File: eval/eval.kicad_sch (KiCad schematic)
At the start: 5 parts, among them J1 TC2030, U9 STM32G0B1CBTx

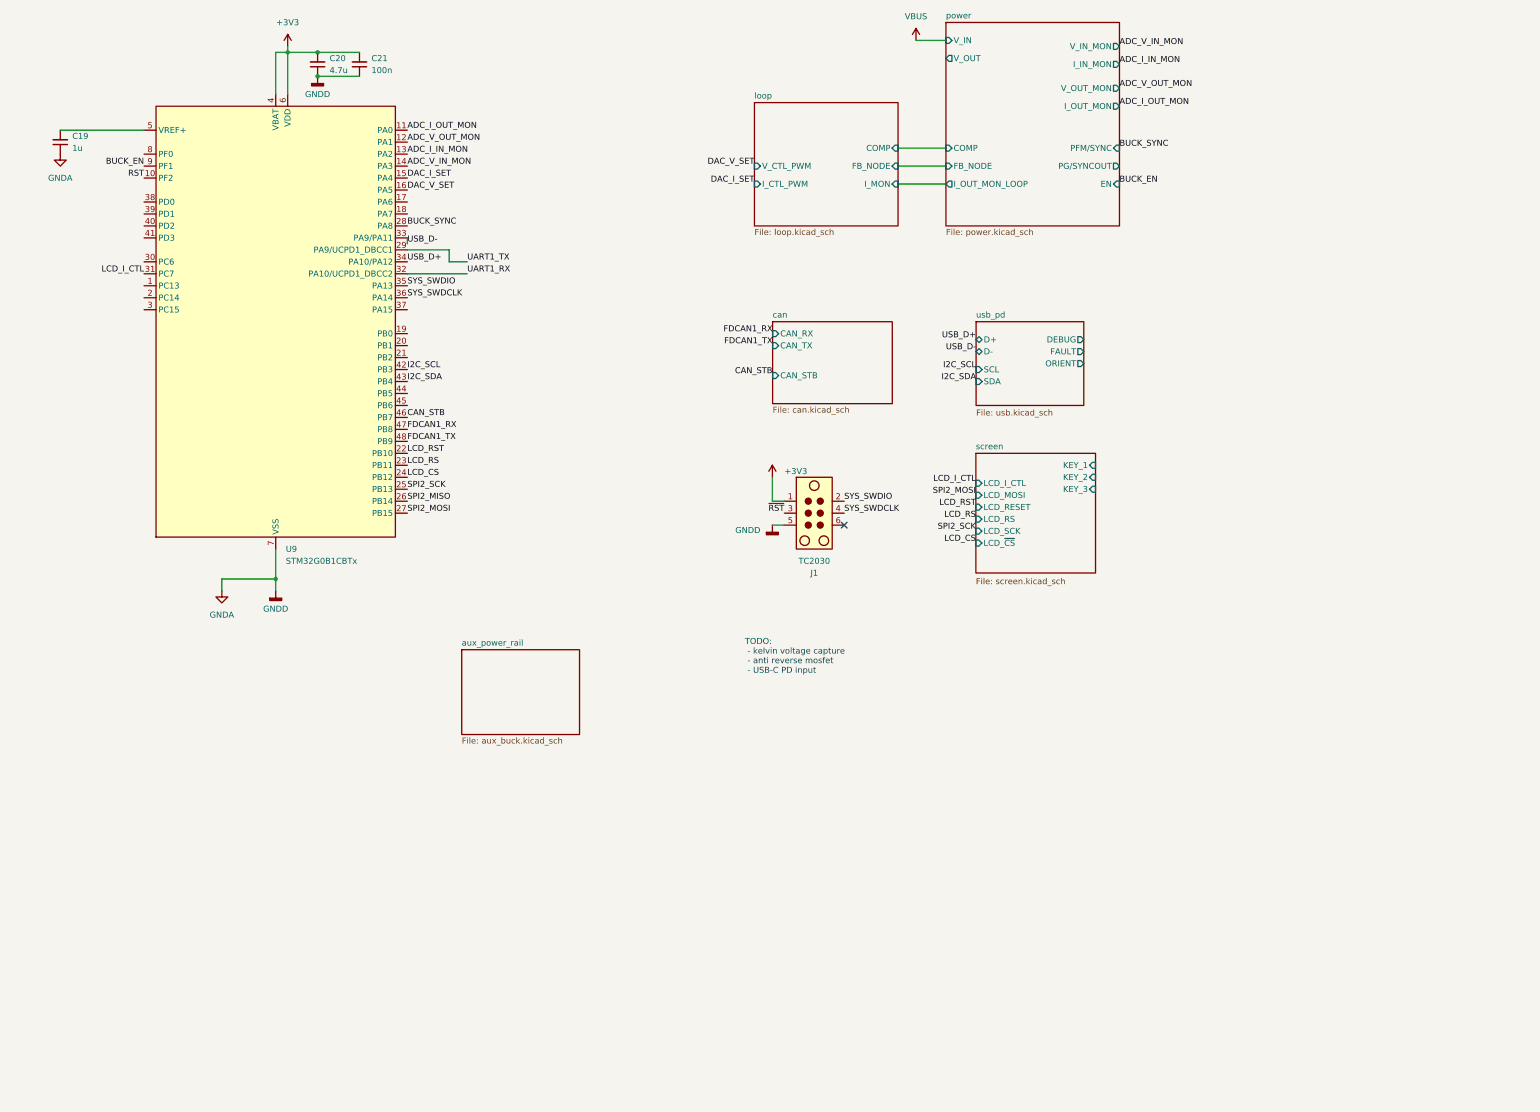
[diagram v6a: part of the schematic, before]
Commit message: [sch] Add ORing for 2 input
plan to add back to back mos protection for output (high side mos)
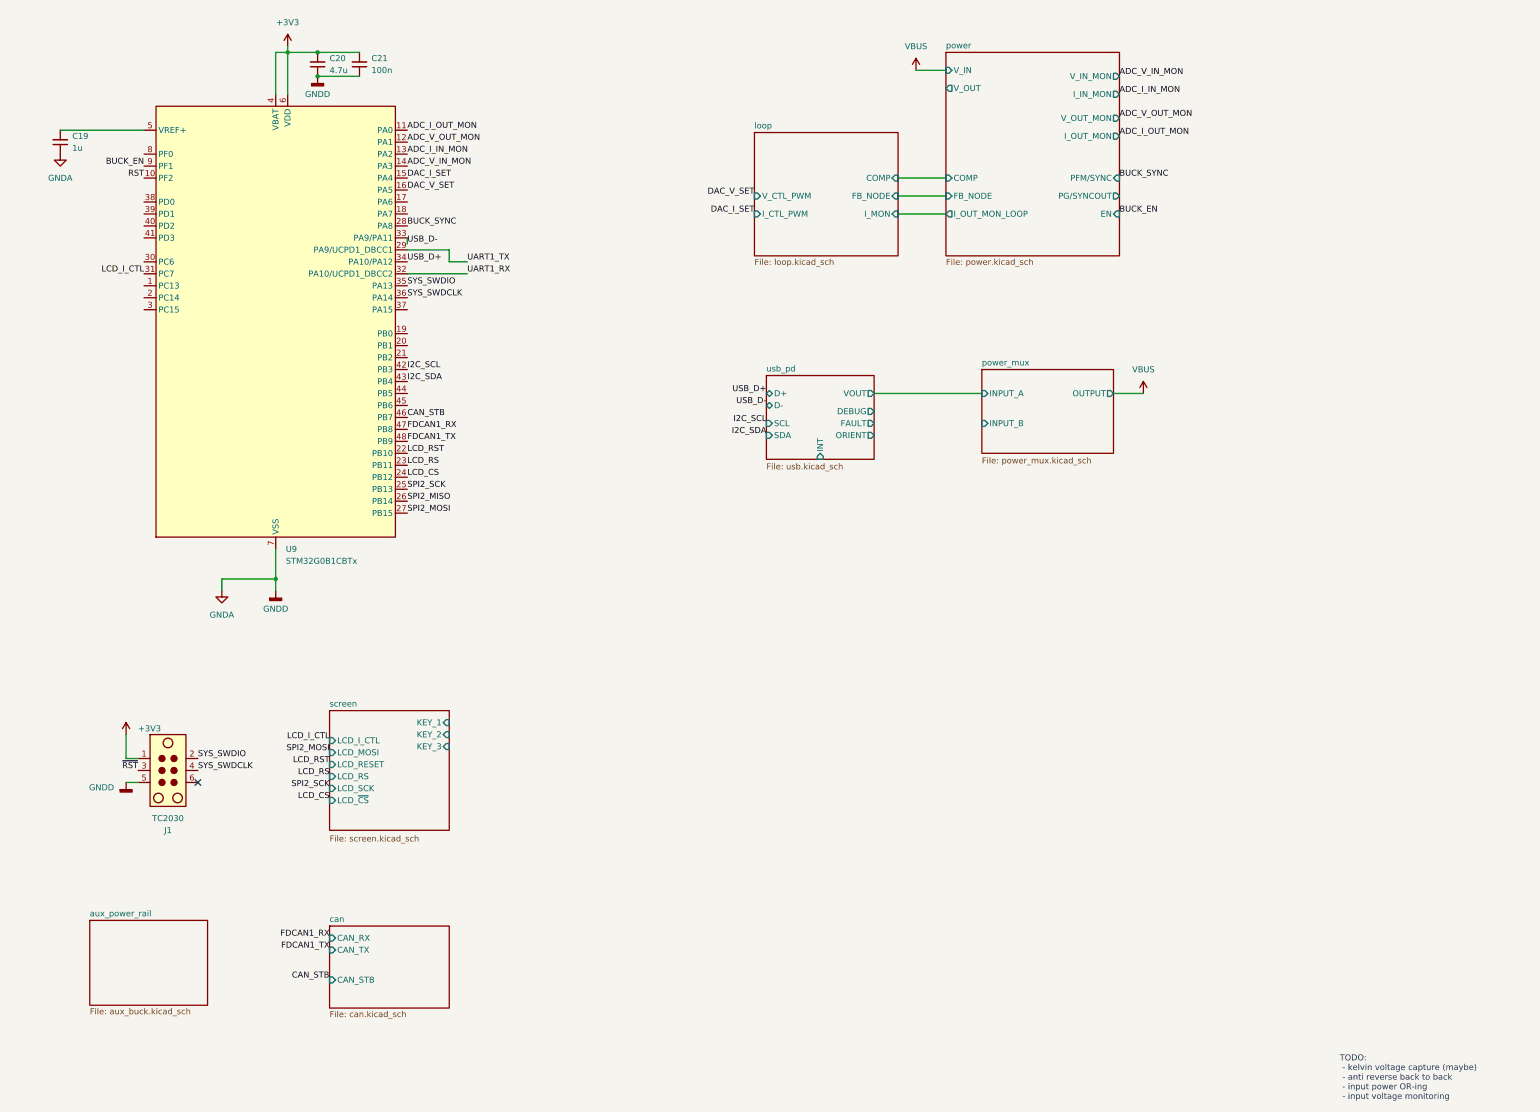
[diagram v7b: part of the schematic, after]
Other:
- added sheet power_mux (power_mux.kicad_sch)
- sheet usb_pd ports: added INT, VOUT; removed none
- note added: "TODO: - kelvin voltage capture (maybe) - anti reverse back to back - input power OR-ing - input voltage monitoring"
- note removed: "TODO: - kelvin voltage capture - anti reverse mosfet - USB-C PD input"
- moved on the sheet: J1

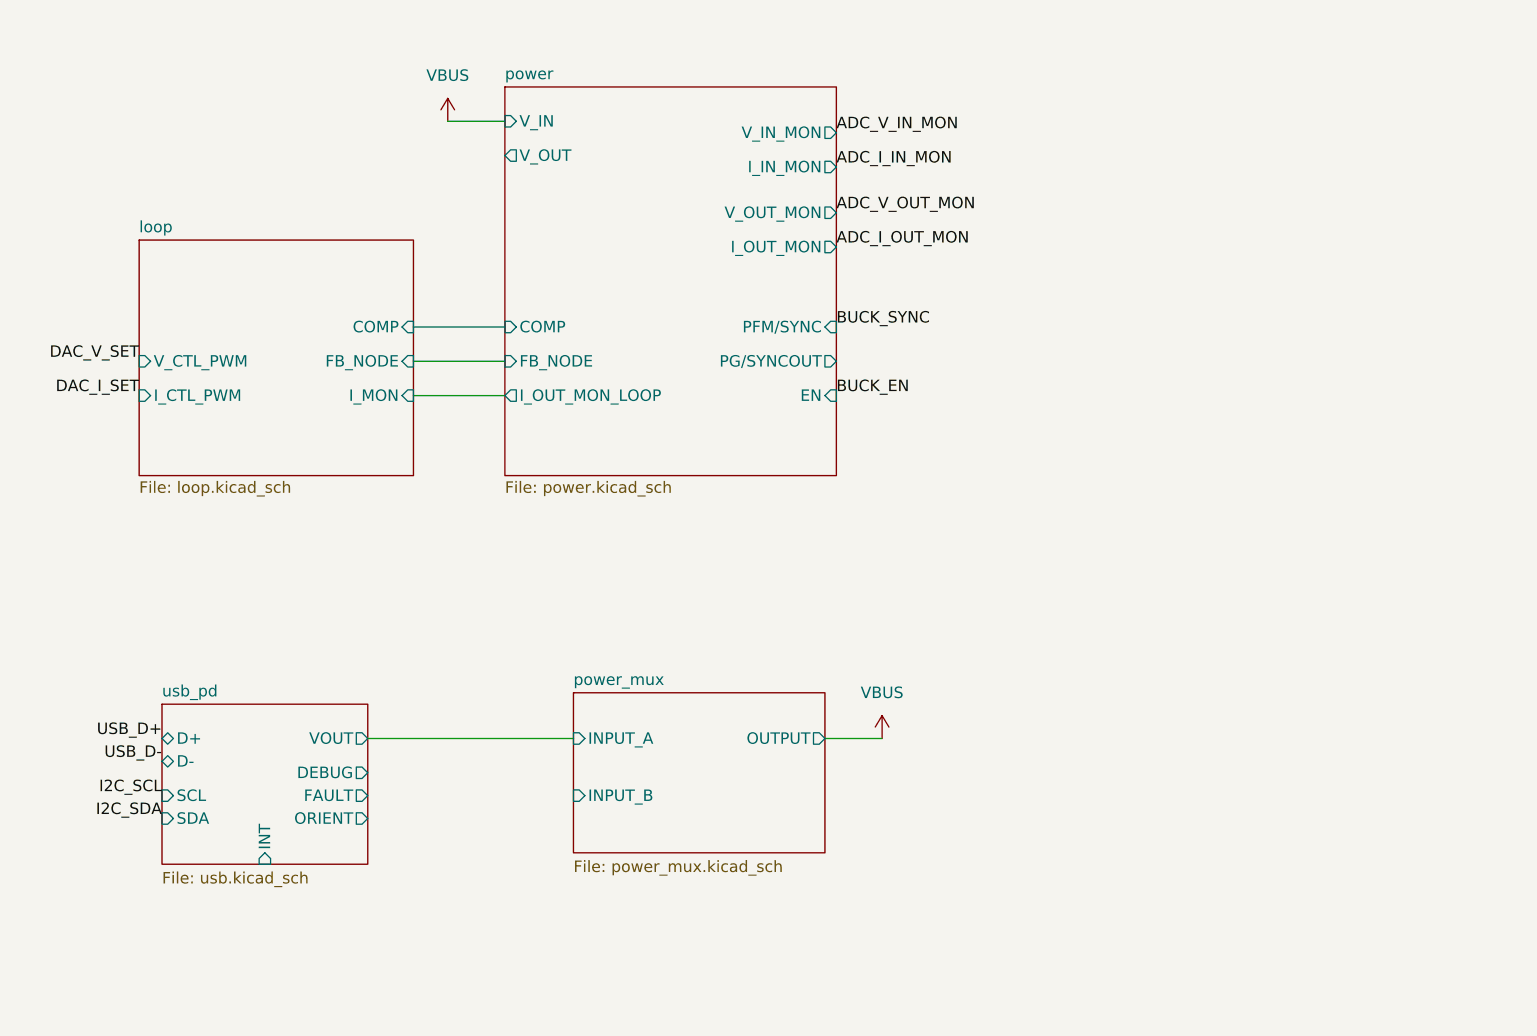
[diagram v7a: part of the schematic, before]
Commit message: [sch] add back to back protection (MX74502)
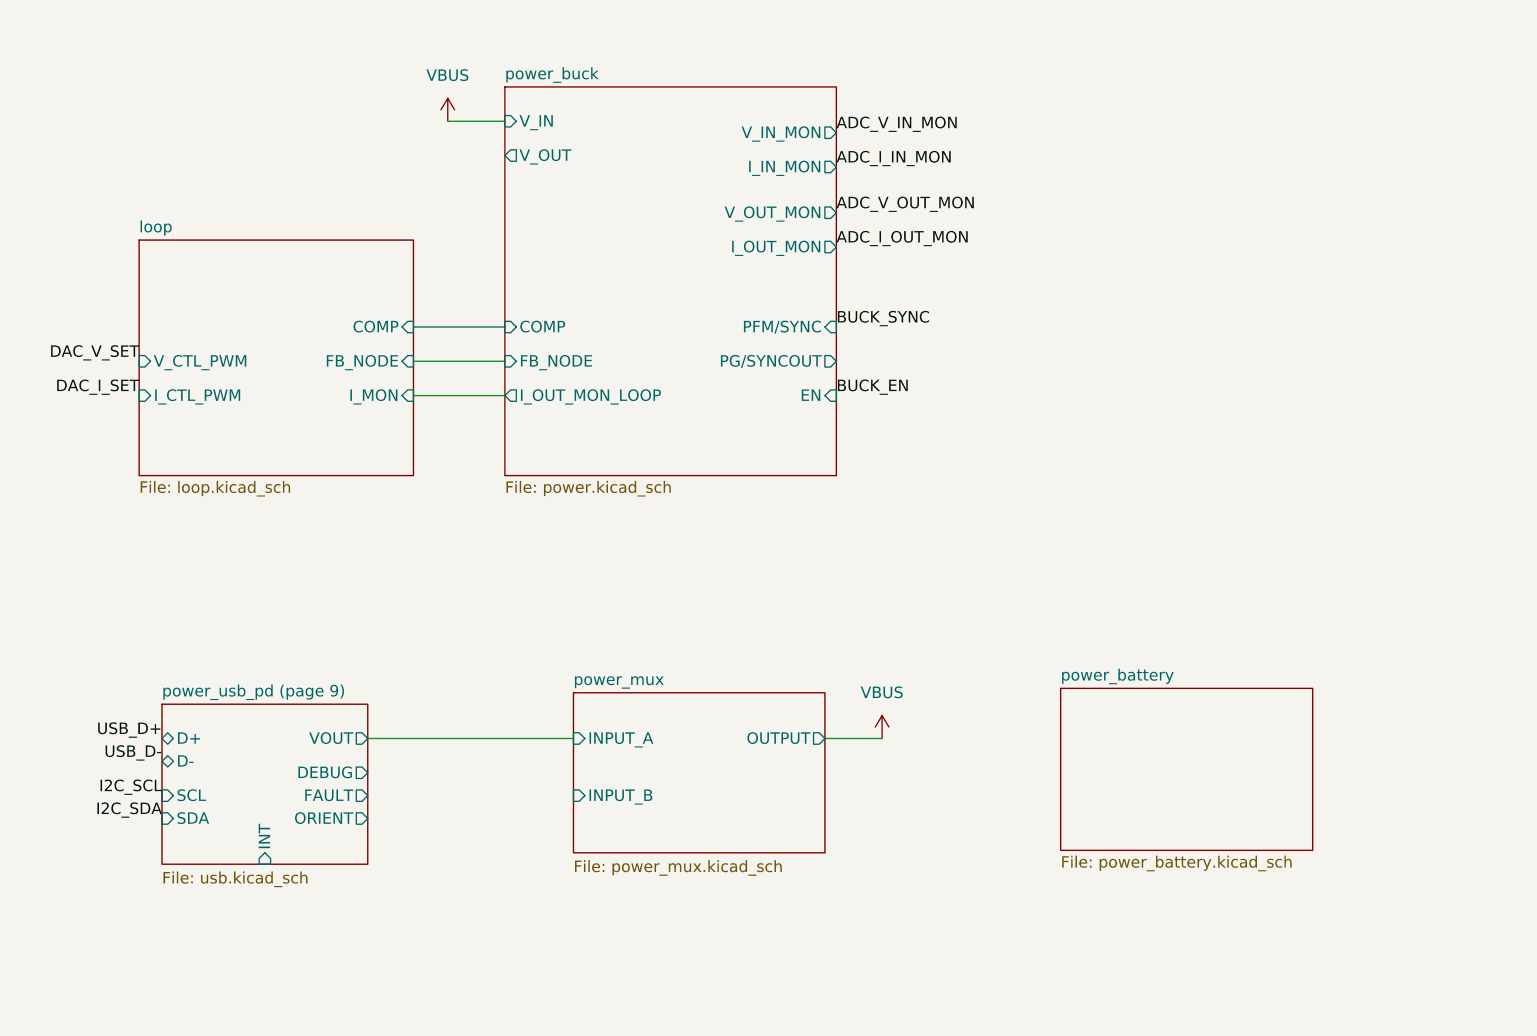
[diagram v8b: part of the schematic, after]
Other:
- sheet power renamed power_buck
- sheet usb_pd renamed power_usb_pd (page 9)
- added sheet power_battery (power_battery.kicad_sch)
